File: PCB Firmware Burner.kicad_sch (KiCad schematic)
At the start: 15 parts, among them J1 Conn_01x06_Male, Q1 BSS138, Q2 BSS138

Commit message: revision 1.1
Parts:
- removed CHC1: 100nF, Capacitor_SMD:C_1206_3216Metric, symbol Device:C
- added QR1, QR2: 10K, Resistor_SMD:R_0805_2012Metric_Pad1.20x1.40mm_HandSolder, symbol Device:R
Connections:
- net CH3V3: no longer LDR1.1
- net at CH340K1.4 (~{DTR}), Q1.2 (S): now also QR2.1; no longer Q2.1 (G)
- net at CH340K1.6 (RTS), Q2.2 (S): now also QR1.1; no longer Q1.1 (G)
- new net: Q2.1 (G), QR2.2
- new net: Q1.1 (G), QR1.2
- new net 3V3: LDR1.1
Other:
- moved on the sheet: Q1, Q2
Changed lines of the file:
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@@
   (junction (at 219.71 82.55) (diameter 0) (color 0 0 0 0)
   )
+  (junction (at 110.998 84.836) (diameter 0) (color 0 0 0 0)
+  )
+  (junction (at 113.538 97.536) (diameter 0) (color 0 0 0 0)
+  )
   (junction (at 181.61 91.44) (diameter 0) (color 0 0 0 0)
   )
-  (junction (at 110.998 84.836) (diameter 0) (color 0 0 0 0)
-  )
   (junction (at 181.61 99.06) (diameter 0) (color 0 0 0 0)
   )
   (junction (at 224.79 82.55) (diameter 0) (color 0 0 0 0)
   )
-  (junction (at 113.538 97.536) (diameter 0) (color 0 0 0 0)
-  )
   (junction (at 215.9 74.93) (diameter 0) (color 0 0 0 0)
-  )
-  (junction (at 136.398 79.756) (diameter 0) (color 0 0 0 0)
   )
   (junction (at 94.488 67.056) (diameter 0) (color 0 0 0 0)
@@
     (stroke (width 0) (type default) (color 0 0 0 0))
   )
-  (wire (pts (xy 123.698 79.756) (xy 136.398 79.756))
+  (wire (pts (xy 132.334 79.756) (xy 143.764 79.756))
     (stroke (width 0) (type default) (color 0 0 0 0))
   )
@@
     (stroke (width 0) (type default) (color 0 0 0 0))
   )
-  (wire (pts (xy 123.698 92.456) (xy 110.998 92.456))
+  (wire (pts (xy 110.998 92.456) (xy 132.334 92.456))
     (stroke (width 0) (type default) (color 0 0 0 0))
   )
@@
     (stroke (width 0) (type default) (color 0 0 0 0))
   )
-  (wire (pts (xy 123.698 102.616) (xy 142.748 102.616))
+  (wire (pts (xy 132.334 102.616) (xy 137.414 102.616))
     (stroke (width 0) (type default) (color 0 0 0 0))
   )
@@
     (stroke (width 0) (type default) (color 0 0 0 0))
   )
-  (wire (pts (xy 113.538 97.536) (xy 116.078 97.536))
-    (stroke (width 0) (type default) (color 0 0 0 0))
-  )
   (wire (pts (xy 107.188 74.676) (xy 104.648 74.676))
     (stroke (width 0) (type default) (color 0 0 0 0))
@@
     (stroke (width 0) (type default) (color 0 0 0 0))
   )
+  (wire (pts (xy 110.998 84.836) (xy 117.094 84.836))
+    (stroke (width 0) (type default) (color 0 0 0 0))
+  )
   (polyline (pts (xy 52.578 106.426) (xy 159.258 106.172))
     (stroke (width 0) (type default) (color 0 0 0 0))
@@
     (stroke (width 0) (type default) (color 0 0 0 0))
   )
-  (wire (pts (xy 110.998 84.836) (xy 116.078 84.836))
-    (stroke (width 0) (type default) (color 0 0 0 0))
-  )
   (wire (pts (xy 67.818 81.026) (xy 70.358 81.026))
     (stroke (width 0) (type default) (color 0 0 0 0))
@@
     (stroke (width 0) (type default) (color 0 0 0 0))
   )
-  (wire (pts (xy 113.538 89.916) (xy 123.698 89.916))
-    (stroke (width 0) (type default) (color 0 0 0 0))
-  )
-  (wire (pts (xy 136.398 87.376) (xy 136.398 92.456))
+  (wire (pts (xy 113.538 89.916) (xy 132.334 89.916))
     (stroke (width 0) (type default) (color 0 0 0 0))
   )
@@
     (stroke (width 0) (type default) (color 0 0 0 0))
   )
+  (wire (pts (xy 113.538 97.536) (xy 117.094 97.536))
+    (stroke (width 0) (type default) (color 0 0 0 0))
+  )
   (wire (pts (xy 181.61 83.82) (xy 213.36 83.82))
     (stroke (width 0) (type default) (color 0 0 0 0))
@@
     (stroke (width 0) (type default) (color 0 0 0 0))
   )
-  (wire (pts (xy 136.398 79.756) (xy 142.748 79.756))
-    (stroke (width 0) (type default) (color 0 0 0 0))
-  )
   (wire (pts (xy 185.42 77.47) (xy 185.42 78.74))
     (stroke (width 0) (type default) (color 0 0 0 0))
@@
     (effects (font (size 1.27 1.27)) (justify left bottom))
   )
-  (label "CH3V3" (at 110.998 122.174 180)
+  (label "3V3" (at 110.998 122.174 180)
     (effects (font (size 1.27 1.27)) (justify right bottom))
   )
@@
     (effects (font (size 1.27 1.27)) (justify left bottom))
   )
-  (label "RST_EN_RTS" (at 142.748 79.756 0)
+  (label "RST_EN_RTS" (at 143.764 79.756 0)
     (effects (font (size 1.27 1.27)) (justify left bottom))
   )
@@
     (effects (font (size 1.27 1.27)) (justify left bottom))
   )
-  (label "IO0_BOOT_DTR" (at 142.748 102.616 0)
+  (label "IO0_BOOT_DTR" (at 137.414 102.616 0)
     (effects (font (size 1.27 1.27)) (justify left bottom))
   )
@@
   )
   (label "TX_OUT_3V3" (at 74.422 119.126 0)
-    (effects (font (size 1.27 1.27)) (justify left bottom))
-  )
-  (label "GND" (at 136.398 92.456 0)
     (effects (font (size 1.27 1.27)) (justify left bottom))
   )
@@
     (pin "2")
   )
-  (symbol (lib_id "Transistor_FET:BSS138") (at 121.158 84.836 0) (unit 1)
-    (in_bom yes) (on_board yes)
-    (property "Reference" "Q2" (id 0) (at 126.3396 83.6676 0)
-      (effects (font (size 1.27 1.27)) (justify left))
-    )
-    (property "Value" "BSS138" (id 1) (at 126.3396 85.979 0)
-      (effects (font (size 1.27 1.27)) (justify left))
-    )
-    (property "Footprint" "Package_TO_SOT_SMD:SOT-23" (id 2) (at 126.238 86.741 0)
+  (symbol (lib_id "Transistor_FET:BSS138") (at 129.794 84.836 0) (unit 1)
+    (in_bom yes) (on_board yes)
+    (property "Reference" "Q2" (id 0) (at 132.588 78.74 0)
+      (effects (font (size 1.27 1.27)) (justify left))
+    )
+    (property "Value" "BSS138" (id 1) (at 133.096 81.026 0)
+      (effects (font (size 1.27 1.27)) (justify left))
+    )
+    (property "Footprint" "Package_TO_SOT_SMD:SOT-23" (id 2) (at 134.874 86.741 0)
       (effects (font (size 1.27 1.27) italic) (justify left) hide)
     )
-    (property "Datasheet" "https://www.onsemi.com/pub/Collateral/BSS138-D.PDF" (id 3) (at 121.158 84.836 0)
+    (property "Datasheet" "https://www.onsemi.com/pub/Collateral/BSS138-D.PDF" (id 3) (at 129.794 84.836 0)
       (effects (font (size 1.27 1.27)) (justify left) hide)
     )
@@
     (pin "6")
   )
+  (symbol (lib_id "Device:R") (at 120.904 84.836 90) (unit 1)
+    (in_bom yes) (on_board yes)
+    (property "Reference" "QR2" (id 0) (at 123.444 87.376 90)
+      (effects (font (size 1.27 1.27)) (justify left))
+    )
+    (property "Value" "10K" (id 1) (at 123.444 82.296 90)
+      (effects (font (size 1.27 1.27)) (justify left))
+    )
+    (property "Footprint" "Resistor_SMD:R_0805_2012Metric_Pad1.20x1.40mm_HandSolder" (id 2) (at 120.904 86.614 90)
+      (effects (font (size 1.27 1.27)) hide)
+    )
+    (property "Datasheet" "~" (id 3) (at 120.904 84.836 0)
+      (effects (font (size 1.27 1.27)) hide)
+    )
+    (pin "1")
+    (pin "2")
+  )
+  (symbol (lib_id "Device:R") (at 120.904 97.536 90) (unit 1)
+    (in_bom yes) (on_board yes)
+    (property "Reference" "QR1" (id 0) (at 123.444 100.076 90)
+      (effects (font (size 1.27 1.27)) (justify left))
+    )
+    (property "Value" "10K" (id 1) (at 123.444 94.996 90)
+      (effects (font (size 1.27 1.27)) (justify left))
+    )
+    (property "Footprint" "Resistor_SMD:R_0805_2012Metric_Pad1.20x1.40mm_HandSolder" (id 2) (at 120.904 99.314 90)
+      (effects (font (size 1.27 1.27)) hide)
+    )
+    (property "Datasheet" "~" (id 3) (at 120.904 97.536 0)
+      (effects (font (size 1.27 1.27)) hide)
+    )
+    (pin "1")
+    (pin "2")
+  )
   (symbol (lib_id "Device:R") (at 114.808 122.174 90) (unit 1)
     (in_bom yes) (on_board yes)
@@
     )
     (property "Datasheet" "~" (id 3) (at 114.808 122.174 0)
-      (effects (font (size 1.27 1.27)) hide)
-    )
-    (pin "1")
-    (pin "2")
-  )
-  (symbol (lib_id "Device:C") (at 136.398 83.566 0) (unit 1)
-    (in_bom yes) (on_board yes)
-    (property "Reference" "CHC1" (id 0) (at 137.668 88.646 0)
-      (effects (font (size 1.27 1.27)) (justify left))
-    )
-    (property "Value" "100nF" (id 1) (at 137.668 86.106 0)
-      (effects (font (size 1.27 1.27)) (justify left))
-    )
-    (property "Footprint" "Capacitor_SMD:C_1206_3216Metric" (id 2) (at 137.3632 87.376 0)
-      (effects (font (size 1.27 1.27)) hide)
-    )
-    (property "Datasheet" "~" (id 3) (at 136.398 83.566 0)
       (effects (font (size 1.27 1.27)) hide)
     )
@@
     (pin "2")
   )
-  (symbol (lib_id "Transistor_FET:BSS138") (at 121.158 97.536 0) (mirror x) (unit 1)
-    (in_bom yes) (on_board yes)
-    (property "Reference" "Q1" (id 0) (at 126.3396 96.3676 0)
-      (effects (font (size 1.27 1.27)) (justify left))
-    )
-    (property "Value" "BSS138" (id 1) (at 126.3396 98.679 0)
-      (effects (font (size 1.27 1.27)) (justify left))
-    )
-    (property "Footprint" "Package_TO_SOT_SMD:SOT-23" (id 2) (at 126.238 95.631 0)
+  (symbol (lib_id "Transistor_FET:BSS138") (at 129.794 97.536 0) (mirror x) (unit 1)
+    (in_bom yes) (on_board yes)
+    (property "Reference" "Q1" (id 0) (at 134.9756 96.3676 0)
+      (effects (font (size 1.27 1.27)) (justify left))
+    )
+    (property "Value" "BSS138" (id 1) (at 134.9756 98.679 0)
+      (effects (font (size 1.27 1.27)) (justify left))
+    )
+    (property "Footprint" "Package_TO_SOT_SMD:SOT-23" (id 2) (at 134.874 95.631 0)
       (effects (font (size 1.27 1.27) italic) (justify left) hide)
     )
-    (property "Datasheet" "https://www.onsemi.com/pub/Collateral/BSS138-D.PDF" (id 3) (at 121.158 97.536 0)
+    (property "Datasheet" "https://www.onsemi.com/pub/Collateral/BSS138-D.PDF" (id 3) (at 129.794 97.536 0)
       (effects (font (size 1.27 1.27)) (justify left) hide)
     )
@@
       (reference "CH340K1") (unit 1) (value "CH340K1") (footprint "Package_SO:SSOP-10_3.9x4.9mm_P1.00mm")
     )
-    (path "/a466de1d-36b0-46d6-93b2-e5c2a1a969d4"
-      (reference "CHC1") (unit 1) (value "100nF") (footprint "Capacitor_SMD:C_1206_3216Metric")
-    )
     (path "/162b7b2e-4a99-4aca-941b-9427ad52cd61"
       (reference "D1") (unit 1) (value "LED") (footprint "LED_SMD:LED_1206_3216Metric")
@@
       (reference "Q2") (unit 1) (value "BSS138") (footprint "Package_TO_SOT_SMD:SOT-23")
     )
+    (path "/812c67fc-7f0e-4057-a362-3d703aefb2f4"
+      (reference "QR1") (unit 1) (value "10K") (footprint "Resistor_SMD:R_0805_2012Metric_Pad1.20x1.40mm_HandSolder")
+    )
+    (path "/44f53c40-3ad5-4a00-98d1-94c4b5c910be"
+      (reference "QR2") (unit 1) (value "10K") (footprint "Resistor_SMD:R_0805_2012Metric_Pad1.20x1.40mm_HandSolder")
+    )
     (path "/1cb2323b-afdb-4617-afef-75823044dc90"

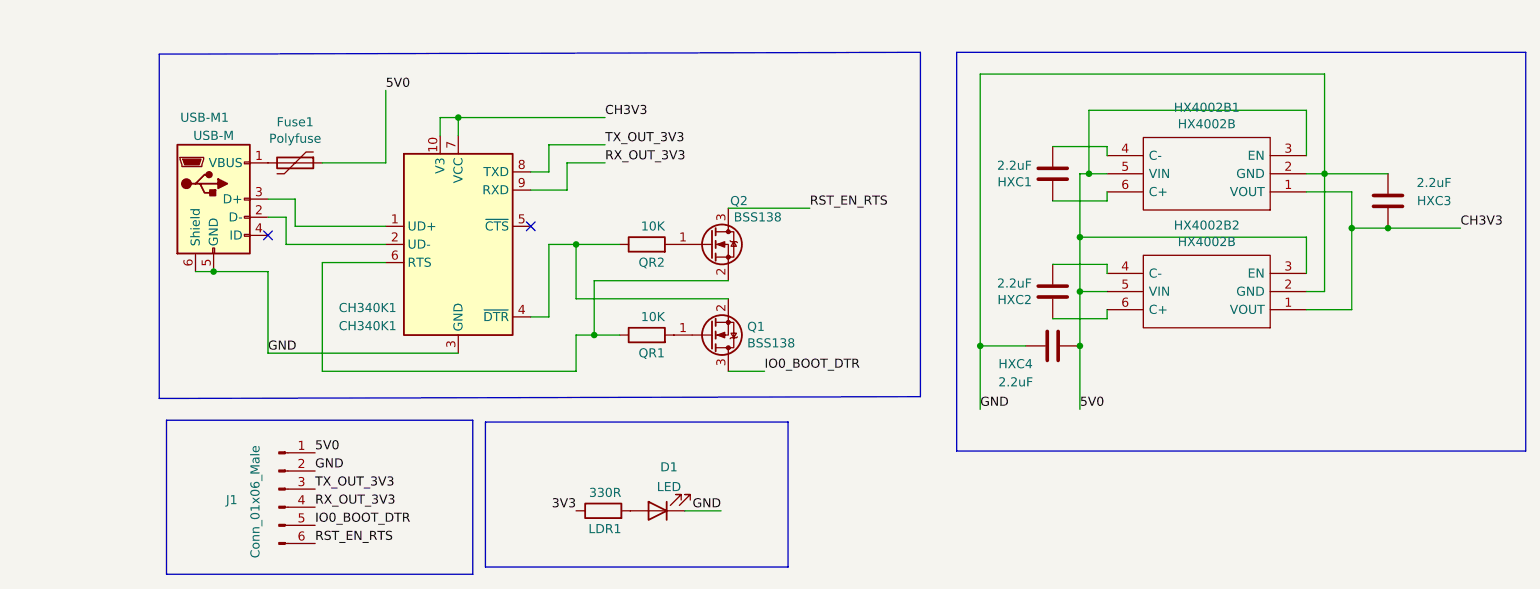
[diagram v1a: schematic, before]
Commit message: revision 1.2
possibility of voltage selection: 3V3 or 5V0
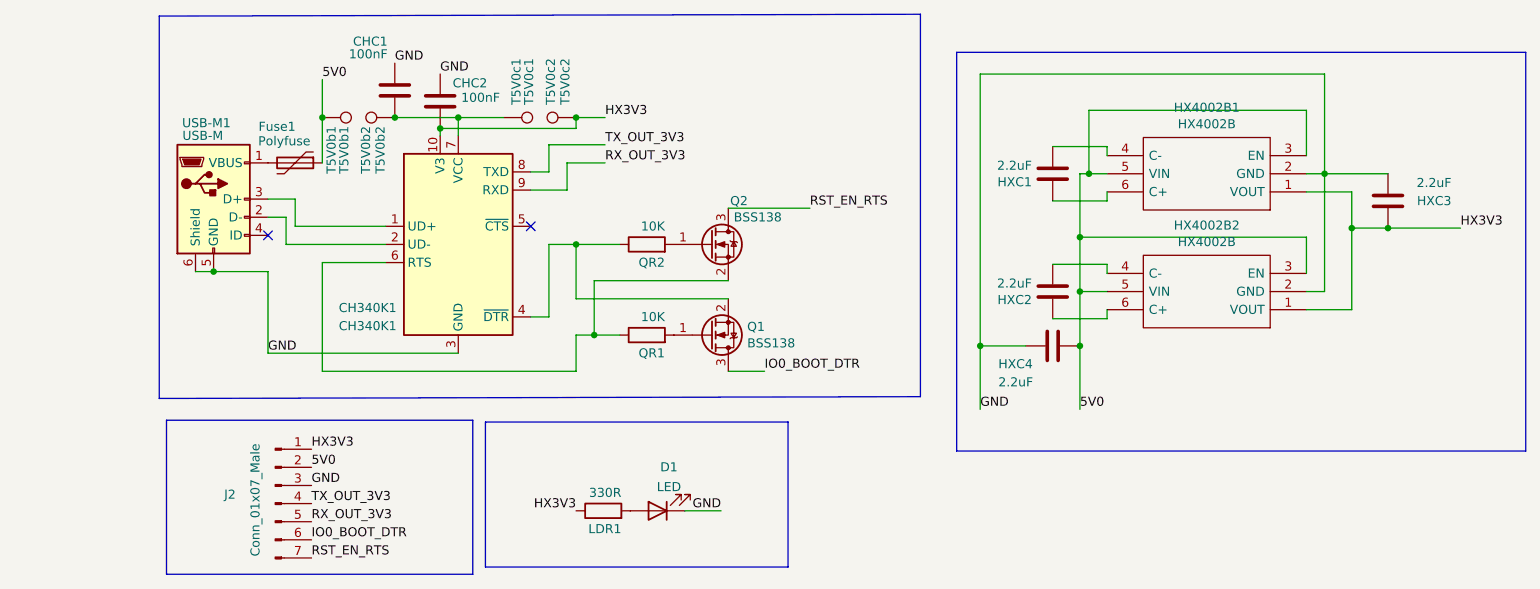
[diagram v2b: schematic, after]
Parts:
- removed J1: Conn_01x06_Male, TerminalBlock_Phoenix:TerminalBlock_Phoenix_MPT-0,5-6-2.54_1x06_P2.54mm_Horizontal, symbol Connector:Conn_01x06_Male
- added CHC1, CHC2: 100nF, Capacitor_SMD:C_1206_3216Metric, symbol Device:C
- added J2: Conn_01x07_Male, TerminalBlock_Phoenix:TerminalBlock_Phoenix_MPT-0,5-7-2.54_1x07_P2.54mm_Horizontal, symbol Connector:Conn_01x07_Male
- added T5V0b1: T5V0b1, TestPoint:TestPoint_Pad_2.0x2.0mm, symbol Connector:TestPoint
- added T5V0b2: T5V0b2, TestPoint:TestPoint_Pad_2.0x2.0mm, symbol Connector:TestPoint
- added T5V0c1: T5V0c1, TestPoint:TestPoint_Pad_2.0x2.0mm, symbol Connector:TestPoint
- added T5V0c2: T5V0c2, TestPoint:TestPoint_Pad_2.0x2.0mm, symbol Connector:TestPoint
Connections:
- net 5V0: now also J2.2 (Pin_2), T5V0b1.1
- net GND: now also CHC1.2, CHC2.2, J2.3 (Pin_3)
- net IO0_BOOT_DTR: now also J2.6 (Pin_6)
- net RST_EN_RTS: now also J2.7 (Pin_7)
- net RX_OUT_3V3: now also J2.5 (Pin_5)
- net TX_OUT_3V3: now also J2.4 (Pin_4)
- net 3V3 renamed HX3V3
- net HX3V3: now also CH340K1.10 (V3), HX4002B1.1 (VOUT), HX4002B2.1 (VOUT), HXC3.1, CHC2.1, J2.1 (Pin_1), T5V0c2.1
- removed net CH3V3: CH340K1.10 (V3), CH340K1.7 (VCC), HX4002B1.1 (VOUT), HX4002B2.1 (VOUT), HXC3.1
- new net: CH340K1.7 (VCC), CHC1.1, T5V0b2.1, T5V0c1.1

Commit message: rev 1.4
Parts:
- added TP3, TP4: TP_3Pole, TestPoint:TestPoint_Pad_1.5mm 3 points, symbol Connector:TestPoint_3Pole
- J2: footprint TerminalBlock_Phoenix:TerminalBlock_Phoenix_MPT-0,5-7-2.54_1x07_P2.54mm_Horizontal -> Connector_PinHeader_2.54mm:PinHeader_1x07_P2.54mm_Horizontal
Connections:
- net GND: no longer USB-M1.6 (Shield)
- net RX_OUT_3V3: now also TP4.3
- net TX_OUT_3V3: now also TP3.3
- net at CH340K1.1 (UD+): now also TP3.2; no longer USB-M1.3 (D+)
- net at CH340K1.2 (UD-): now also TP4.2; no longer USB-M1.2 (D-)
- new net: TP4.1, USB-M1.2 (D-)
- new net: TP3.1, USB-M1.3 (D+)
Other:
- moved on the sheet: J2, USB-M1
